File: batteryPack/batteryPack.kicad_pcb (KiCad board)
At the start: 2 copper layers, 2 parts, among them U1 TP5100-Module

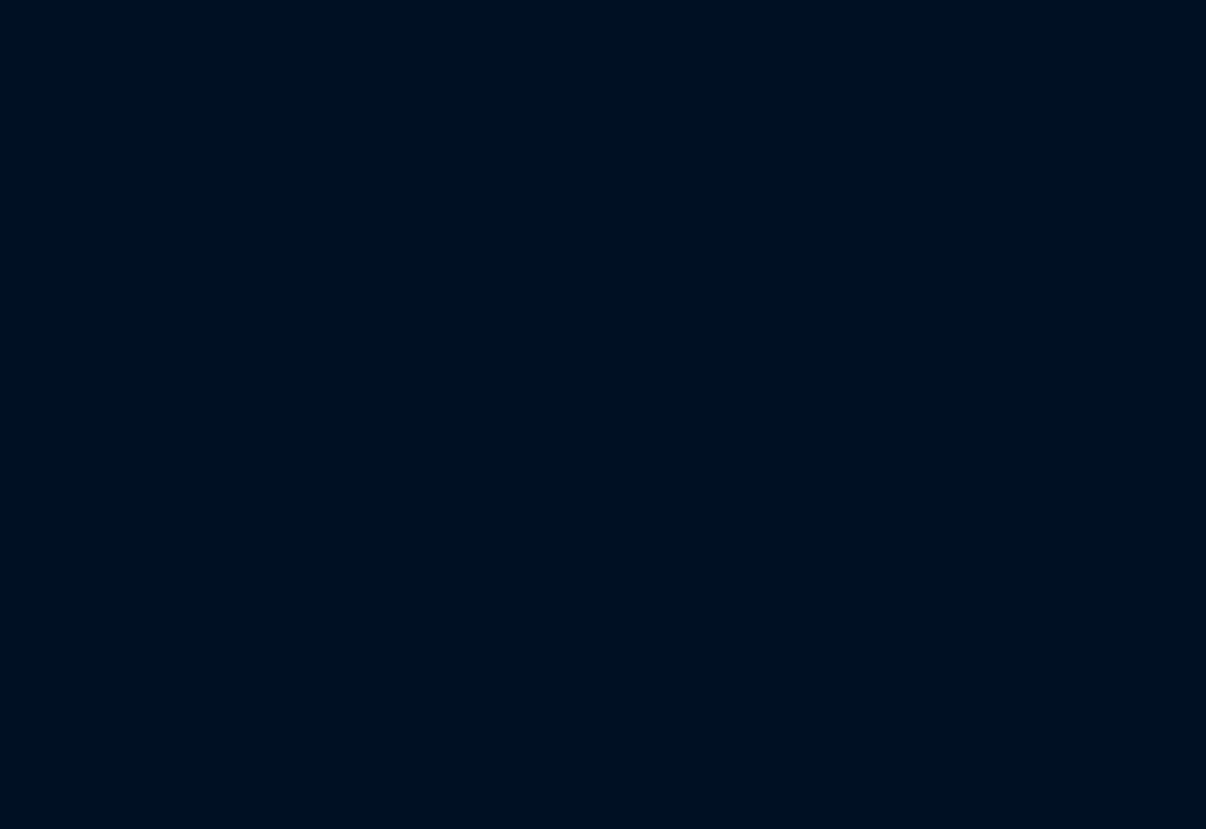
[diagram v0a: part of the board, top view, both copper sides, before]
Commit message: Finish first draft of the schematics
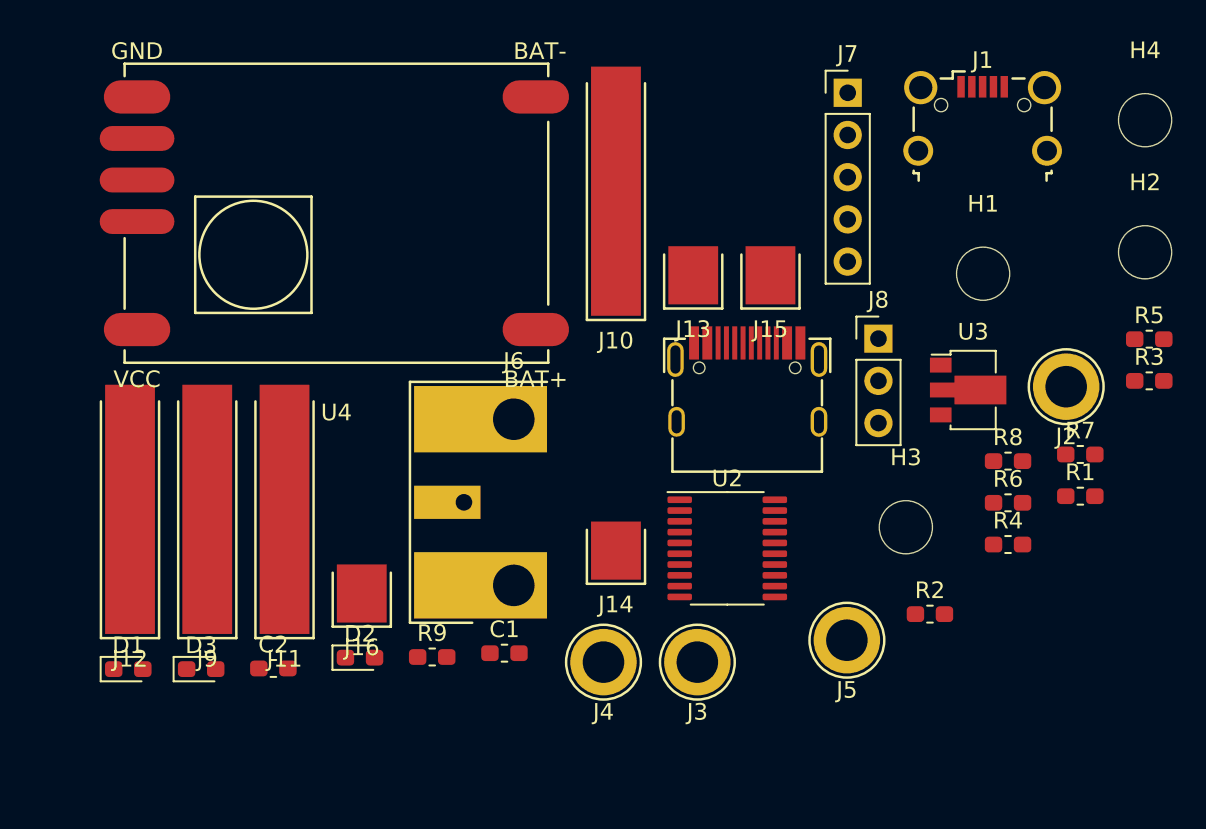
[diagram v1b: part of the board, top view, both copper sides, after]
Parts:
- added C1: 470n, Capacitor_SMD:C_0603_1608Metric_Pad1.05x0.95mm_HandSolder, F.Cu at (230.0, 65.0)
- added C2: 470n, Capacitor_SMD:C_0603_1608Metric_Pad1.05x0.95mm_HandSolder, F.Cu at (216.1, 65.9)
- added D1: LED_5V, LED_SMD:LED_0603_1608Metric_Pad1.05x0.95mm_HandSolder, F.Cu at (207.4, 66.0)
- added D2: LED_9V, LED_SMD:LED_0603_1608Metric_Pad1.05x0.95mm_HandSolder, F.Cu at (221.3, 65.3)
- added D3: LED_12V, LED_SMD:LED_0603_1608Metric_Pad1.05x0.95mm_HandSolder, F.Cu at (211.7, 66.0)
- added H1: MountingHole, MountingHole:MountingHole_3.2mm_M3, F.Cu at (258.8, 42.2)
- added H2: MountingHole, MountingHole:MountingHole_3.2mm_M3, F.Cu at (268.6, 40.9)
- added H3: MountingHole, MountingHole:MountingHole_3.2mm_M3, F.Cu at (254.2, 57.4)
- added H4: MountingHole, MountingHole:MountingHole_3.2mm_M3, F.Cu at (268.6, 32.9)
- added J1: USB_B_Micro, Connector_USB:USB_Micro-B_Wuerth_629105150521_CircularHoles, F.Cu at (258.8, 32.8)
- added J10: B1+, batteryPack:2mm_Banana-Socket, F.Cu at (236.7, 29.7)
- added J11: B1-, batteryPack:2mm_Banana-Socket, F.Cu at (216.8, 48.8)
- added J12: B2-, batteryPack:2mm_Banana-Socket, F.Cu at (207.5, 48.8)
- added J13: B1+, batteryPack:2mm_Banana-Plug, F.Cu at (241.4, 40.5)
- added J14: B1-, batteryPack:2mm_Banana-Plug, F.Cu at (236.7, 57.1)
- added J15: B2+, batteryPack:2mm_Banana-Plug, F.Cu at (246.0, 40.5)
- added J16: B2-, batteryPack:2mm_Banana-Plug, F.Cu at (221.4, 59.7)
- added J2: B1+, batteryPack:2mm_Banana-Vertical, F.Cu at (263.8, 49.0)
- added J3: B1-, batteryPack:2mm_Banana-Vertical, F.Cu at (241.6, 65.5)
- added J4: B2-, batteryPack:2mm_Banana-Vertical, F.Cu at (236.0, 65.5)
- added J5: B2+, batteryPack:2mm_Banana-Vertical, F.Cu at (250.6, 64.2)
- added J6: Conn_01x03, batteryPack:cableConnector, F.Cu at (230.6, 55.9)
- added J7: SWD, Connector_PinHeader_2.54mm:PinHeader_1x05_P2.54mm_Vertical, F.Cu at (250.7, 31.3)
- added J8: UART, Connector_PinHeader_2.54mm:PinHeader_1x03_P2.54mm_Vertical, F.Cu at (252.5, 46.1)
- added J9: B2+, batteryPack:2mm_Banana-Socket, F.Cu at (212.1, 48.8)
- added P1: USB_C_Plug_USB2.0, batteryPack:USB_C_Female-16Pin-HPJF, F.Cu at (244.6, 46.3)
- added R1: 10k, Resistor_SMD:R_0603_1608Metric_Pad1.05x0.95mm_HandSolder, F.Cu at (264.7, 55.5)
- added R2: 2k4, Resistor_SMD:R_0603_1608Metric_Pad1.05x0.95mm_HandSolder, F.Cu at (255.6, 62.6)
- added R3: 10k, Resistor_SMD:R_0603_1608Metric_Pad1.05x0.95mm_HandSolder, F.Cu at (268.8, 48.6)
- added R4: 2k4, Resistor_SMD:R_0603_1608Metric_Pad1.05x0.95mm_HandSolder, F.Cu at (260.3, 58.5)
- added R5: 1k, Resistor_SMD:R_0603_1608Metric_Pad1.05x0.95mm_HandSolder, F.Cu at (268.8, 46.1)
- added R6: 1k, Resistor_SMD:R_0603_1608Metric_Pad1.05x0.95mm_HandSolder, F.Cu at (260.3, 56.0)
- added R7: 1k, Resistor_SMD:R_0603_1608Metric_Pad1.05x0.95mm_HandSolder, F.Cu at (264.7, 53.0)
- added R8: 62k, Resistor_SMD:R_0603_1608Metric_Pad1.05x0.95mm_HandSolder, F.Cu at (260.3, 53.4)
- added R9: 10k, Resistor_SMD:R_0603_1608Metric_Pad1.05x0.95mm_HandSolder, F.Cu at (225.7, 65.2)
- added U2: STM32F030F4Px, Package_SO:TSSOP-20_4.4x6.5mm_P0.65mm, F.Cu at (243.4, 58.7)
- added U3: HT7533-1, Package_TO_SOT_SMD:SOT-89-3, F.Cu at (257.9, 49.2)
- added U4: TP5100-Module, batteryPack:TP5100-Module, F.Cu at (219.9, 38.5)
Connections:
- BT1 pad 1: (no net) -> Net-(BT1-Pad1)
- BT1 pad 1+: (no net) -> Net-(BT1-Pad1+)
- BT1 pad 2: (no net) -> Net-(BT1-Pad2)
- BT1 pad 2+: (no net) -> Net-(BT1-Pad2+)
- U1 pad 1: (no net) -> GND
- U1 pad 2: (no net) -> VBUS
- U1 pad 3: (no net) -> Net-(J13-Pad1)
- U1 pad 4: (no net) -> Net-(J14-Pad1)

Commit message: Sketch out initial component layout
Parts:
- removed H3, H4: MountingHole, MountingHole:MountingHole_3.2mm_M3
- J6: value Conn_01x03 -> CableConnector
- moved J10 169.4 mm to (70.0, 60.0), turned to 270 degrees
- moved J11 147.9 mm to (70.0, 67.0), turned to 270 degrees
- moved J9 145.5 mm to (70.0, 80.0), turned to 270 degrees
- moved J2 144.2 mm to (120.0, 60.0)
- moved H2 144.2 mm to (131.0, 84.0)
- moved J12 139.6 mm to (70.0, 73.0), turned to 270 degrees
- moved J5 131.6 mm to (120.0, 80.0)
- moved H1 128.6 mm to (131.0, 56.0)
- moved J3 121.6 mm to (120.0, 67.0)
- moved J4 116.2 mm to (120.0, 73.0)
- moved U1 108.6 mm to (208.5, 59.5), turned to 180 degrees
- moved J6 98.1 mm to (133.5, 70.0)
- moved BT1 85.1 mm to (50.0, 70.0), turned to 90 degrees
- moved J15 68.3 mm to (190.2, 80.0), turned to 90 degrees
- moved J7 57.7 mm to (236.8, 87.2), turned to 270 degrees
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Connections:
- net Net-(J2-Pad1) renamed /OUT+
- net Net-(J3-Pad1) renamed /MID
- net Net-(J4-Pad1) renamed /OUT-
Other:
- board outline added: 212 x 78 mm
- board text added: "3mm plywood in the robot"
- board text added: "Battery Connector"
- board text added: "Battery Pack"
- board text added: "Isolation 3mm plywood on the back of the battery pack"
- board text removed: "BatteryPack"

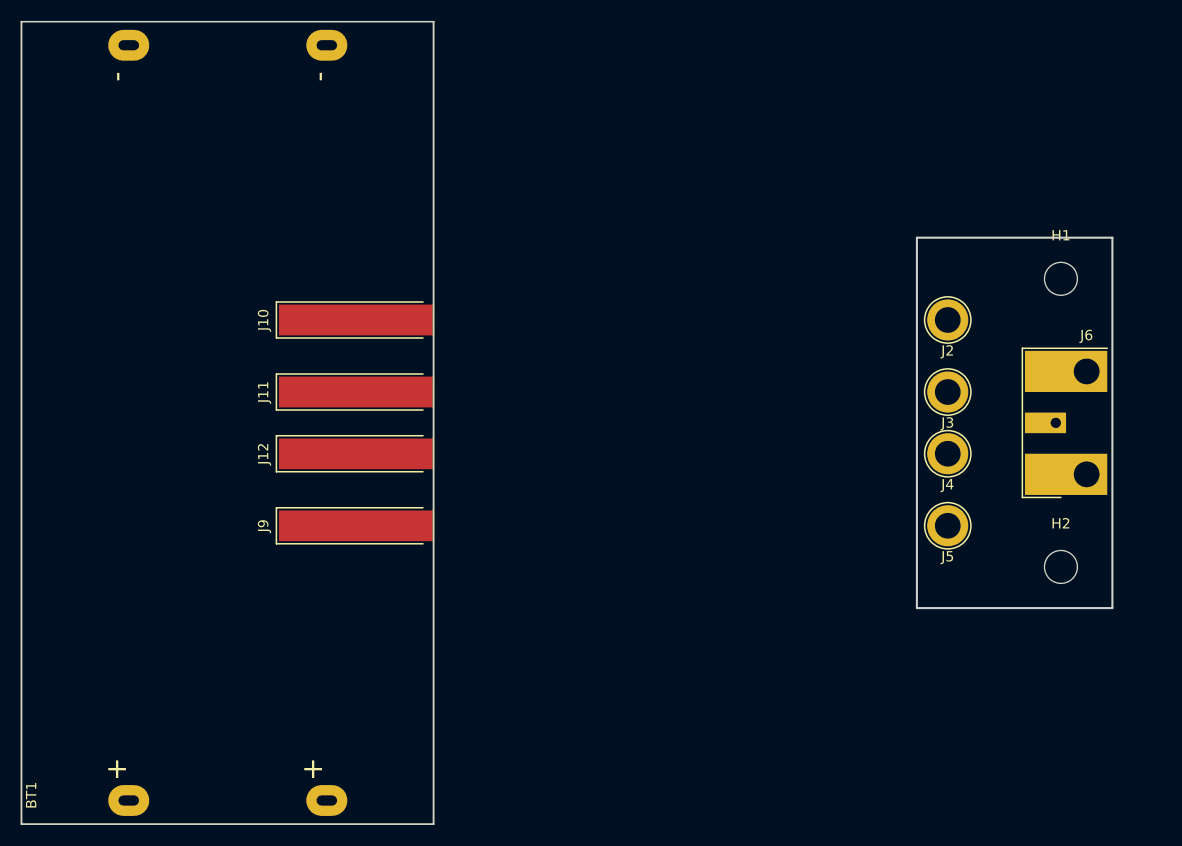
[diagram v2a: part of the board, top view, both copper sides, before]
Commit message: Route battery and the connector
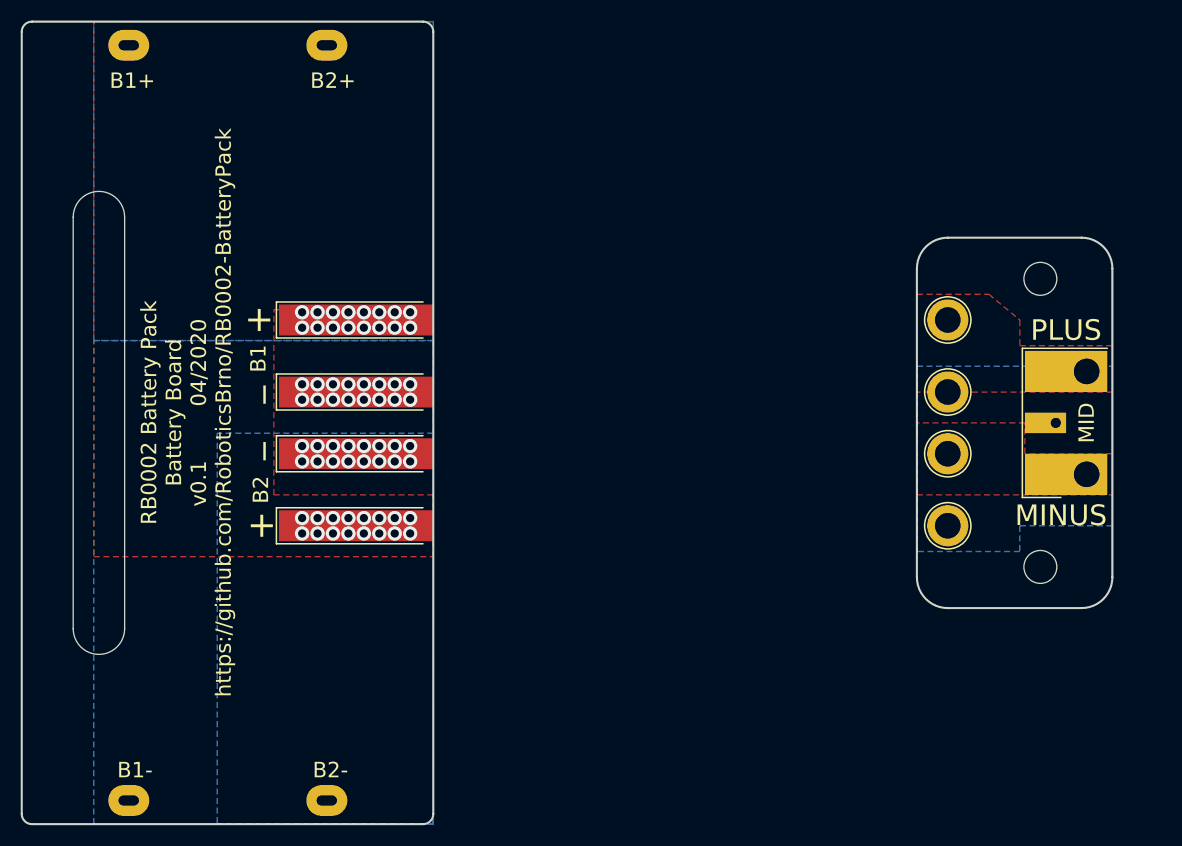
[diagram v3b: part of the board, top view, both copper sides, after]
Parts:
- BT1: moved to B.Cu
- moved H1 2.00 mm to (129.0, 56.0)
- moved H2 2.00 mm to (129.0, 84.0)
- turned BT1 to 270 degrees
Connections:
- net Net-(BT1-Pad1) renamed /BP_B1-
- net Net-(BT1-Pad1+) renamed /BP_B1+
- net Net-(BT1-Pad2) renamed /BP_B2-
- net Net-(BT1-Pad2+) renamed /BP_B2+
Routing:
- net /BP_B2-: vias 0 -> 16
- net /BP_B2+: vias 0 -> 16
- net /BP_B1-: vias 0 -> 16
- net /BP_B1+: vias 0 -> 16
- added copper zone on B.Cu, net /BP_B1+
- added copper zone on B.Cu, net /BP_B1-
- added copper zone on F.Cu, net /BP_B2+
- added copper zone on B.Cu, net /BP_B2-
- added copper zone on B.Cu, net /MID
- added copper zone on F.Cu, net /OUT+
- added copper zone on F.Cu, net /OUT-
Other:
- outline, holes or cut-outs redrawn
- board text added: "+"
- board text added: "0.5 mm for the heat shrink tube"
- board text added: "B1"
- board text added: "B1+"
- board text added: "B1-"
- board text added: "B2"
- board text added: "B2+"
- board text added: "B2-"
- board text added: "MID"
- board text added: "MINUS"
- board text added: "PLUS"
- board text added: "Pull-out strip cutout"
- board text added: "RB0002 Battery Pack Battery Board v0.1 04/2020 https://github.com/RoboticsBrno/RB0002-BatteryPack"
- board text added: "_"

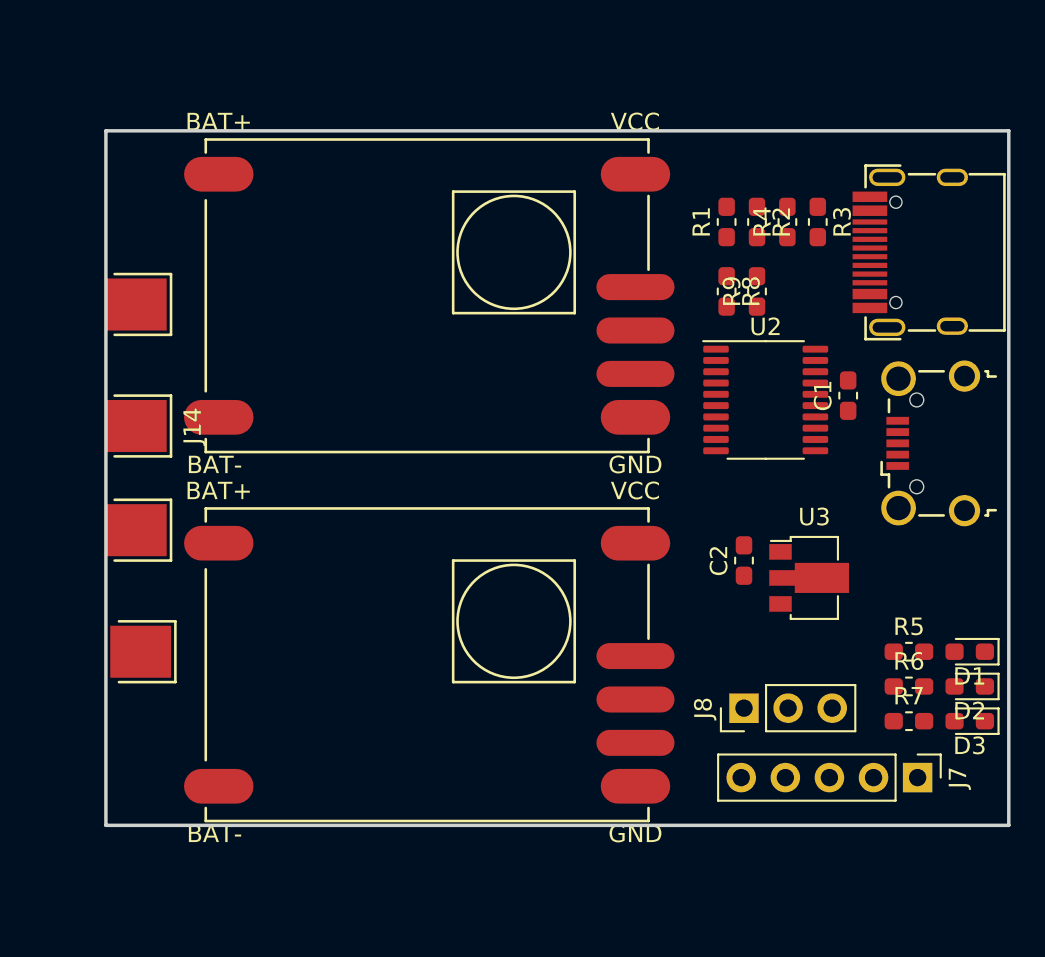
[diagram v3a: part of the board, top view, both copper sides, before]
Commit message: Route the charger
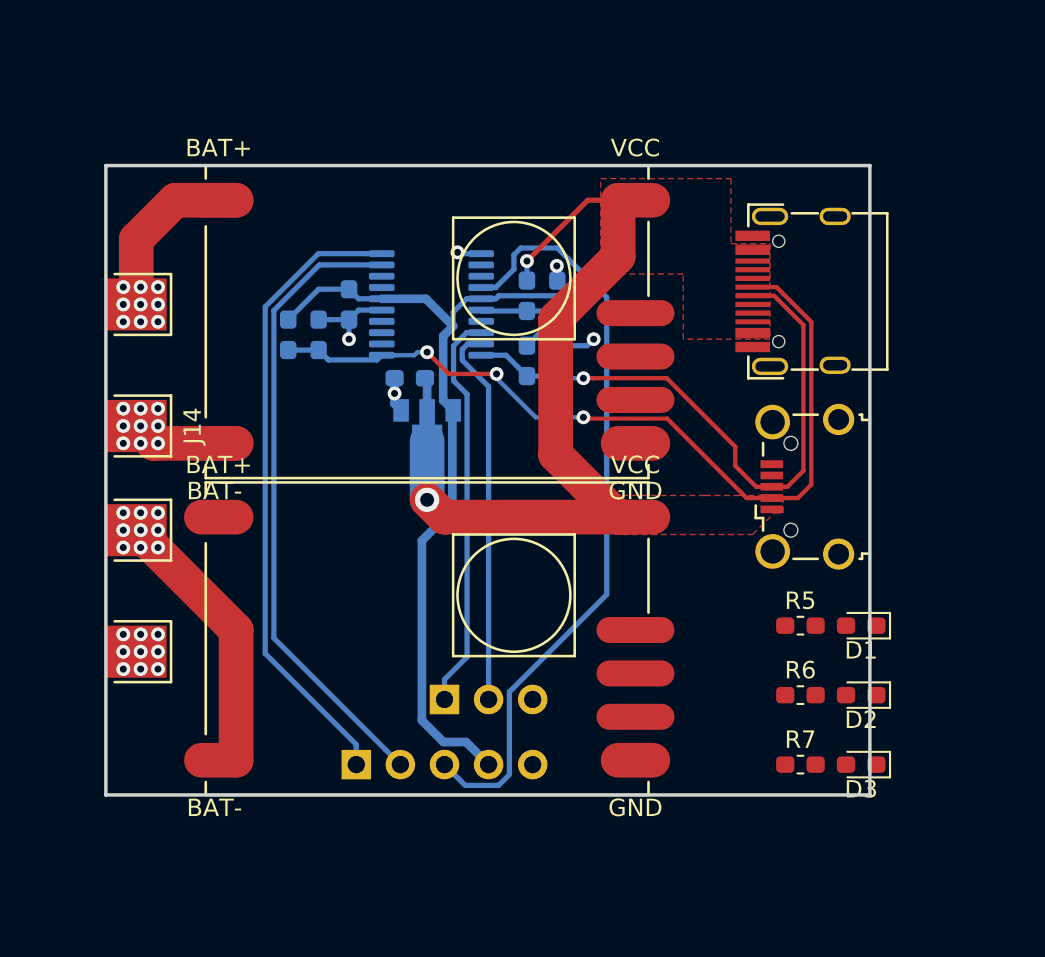
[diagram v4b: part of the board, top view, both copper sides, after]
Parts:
- C1, C2, J7, J8, R1, R2, R3, R4, R8, R9, U2, U3: moved to B.Cu
- moved J7 32.3 mm to (204.4, 86.5)
- moved C1 29.2 mm to (204.0, 60.0)
- moved R1 26.1 mm to (200.5, 61.8), turned to 270 degrees
- moved R2 26.1 mm to (202.2, 61.8), turned to 90 degrees
- moved U3 23.4 mm to (208.5, 67.8), turned to 270 degrees
- moved C2 21.9 mm to (207.5, 64.2), turned to 0 degrees
- moved U2 20.0 mm to (208.8, 60.0), turned to 180 degrees
- moved R3 18.6 mm to (214.2, 63.2)
- moved J8 17.3 mm to (209.5, 82.8), turned to 270 degrees
- moved R4 15.5 mm to (216.0, 63.2)
- moved R8 11.5 mm to (214.2, 59.5)
- moved R9 11.5 mm to (216.0, 59.5)
- moved J1 7.67 mm to (230.2, 70.5)
- moved P1 7.12 mm to (227.2, 59.2)
- moved D3 6.73 mm to (233.5, 86.5)
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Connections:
- J7 pad 1: SWDIO -> SWCLK
- J7 pad 2: SWCLK -> SWDIO
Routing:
- net +3V3: track 0.00 -> 52.4 mm
- net D-: track 0.00 -> 48.1 mm, vias 0 -> 3
- net VBUS: track 0.00 -> 46.7 mm, vias 0 -> 2
- net RST: track 0.00 -> 44.1 mm
- net SWCLK: track 0.00 -> 36.5 mm
- net SWDIO: track 0.00 -> 36.5 mm
- net D+: track 0.00 -> 34.7 mm, vias 0 -> 1
- net TX: track 0.00 -> 23.1 mm
- net RX: track 0.00 -> 22.0 mm
- net Net-(J16-Pad1): track 0.00 -> 15.6 mm, vias 0 -> 9
- net GND: track 0.00 -> 11.5 mm, vias 0 -> 5
- net Net-(J13-Pad1): track 0.00 -> 10.4 mm, vias 0 -> 9
- net Net-(J14-Pad1): track 0.00 -> 6.16 mm, vias 0 -> 9
- net /VBUS_SENSE: track 0.00 -> 4.41 mm
- net Net-(J15-Pad1): vias 0 -> 9
- added copper zone on F.Cu, net VBUS
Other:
- board size 212 x 78 mm -> 204 x 78 mm
